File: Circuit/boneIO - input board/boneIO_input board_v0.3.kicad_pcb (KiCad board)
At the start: 2 copper layers, 256 x 74 mm, 264 parts, among them J1 Screw_Terminal_01x08, J10 Screw_Terminal_01x08, J11 Screw_Terminal_01x08, J12 ZW_VCC, J13 ZW_GND, J14 INNY ZASILACZ, J15 BeagleBone_Black_Header, J16 BeagleBone_Black_Header, J2 Screw_Terminal_01x08, J3 Screw_Terminal_01x08, J4 Screw_Terminal_01x08, J5 Screw_Terminal_01x08, J6 Screw_Terminal_01x08, J7 Screw_Terminal_01x08, J8 Screw_Terminal_01x04, J9 Conn_02x04_Odd_Even, SW1 SW_Push, U1 P82B96, U10 LM2596S-ADJ, U11 RS485, U12 PC817X2NIP0F, U13 PC817X2NIP0F, U14 PC817X2NIP0F, U15 PC817X2NIP0F, U16 PC817X2NIP0F, U17 PC817X2NIP0F, U18 PC817X2NIP0F, U19 PC817X2NIP0F, U2 PC817X2NIP0F, U20 PC817X2NIP0F, U21 PC817X2NIP0F, U22 PC817X2NIP0F, U23 PC817X2NIP0F, U24 PC817X2NIP0F, U25 PC817X2NIP0F, U26 PC817X2NIP0F, U27 PC817X2NIP0F, U28 PC817X2NIP0F, U29 PC817X2NIP0F, U3 PC817X2NIP0F, U30 PC817X2NIP0F, U31 PC817X2NIP0F, U32 PC817X2NIP0F, U33 PC817X2NIP0F, U34 PC817X2NIP0F, U35 PC817X2NIP0F, U36 DS1307Z+, U37 PC817X2NIP0F, U38 PC817X2NIP0F, U39 PC817X2NIP0F, U4 PC817X2NIP0F, U40 PC817X2NIP0F, U41 PC817X2NIP0F, U42 PC817X2NIP0F, U43 PC817X2NIP0F, U44 PC817X2NIP0F, U45 PC817X2NIP0F, U46 PC817X2NIP0F, U47 PC817X2NIP0F, U48 PC817X2NIP0F, U49 PC817X2NIP0F, U5 PC817X2NIP0F, U50 PC817X2NIP0F, U51 PC817X2NIP0F, U52 PC817X2NIP0F, U53 PC817X2NIP0F, U54 PC817X2NIP0F, U55 PC817X2NIP0F, U56 PC817X2NIP0F, U6 PC817X2NIP0F, U7 PC817X2NIP0F, U8 PC817X2NIP0F, U9 PC817X2NIP0F, Y1 32,788 MHz

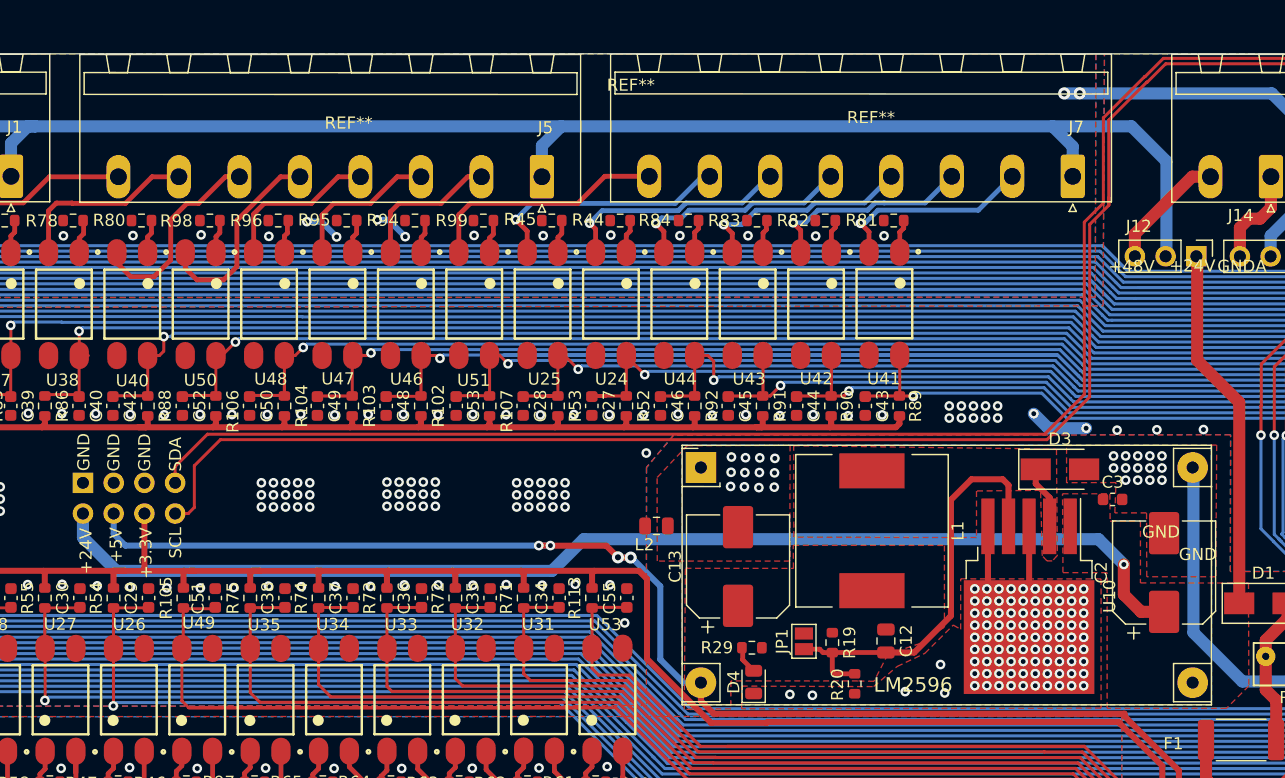
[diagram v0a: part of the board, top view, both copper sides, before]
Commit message: Wymiana gniazda
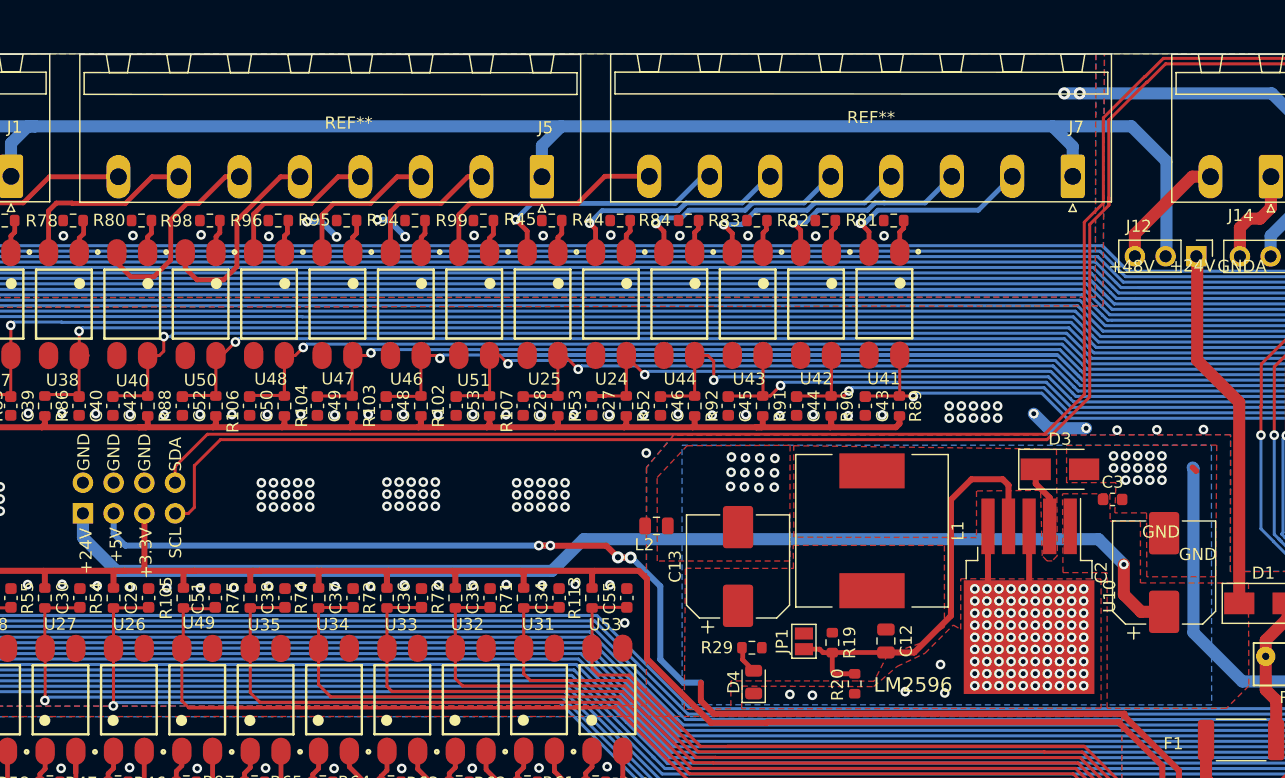
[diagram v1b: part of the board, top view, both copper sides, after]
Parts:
- removed REF**: YAAJ_DCDC_StepDown_LM2596, Module:YAAJ_DCDC_StepDown_LM2596
- J9: footprint Connector_PinHeader_2.54mm:PinHeader_2x04_P2.54mm_Vertical -> Connector_PinSocket_2.54mm:PinSocket_2x04_P2.54mm_Vertical
- moved J9 2.53 mm to (109.6, 84.3)
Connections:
- J9 pad 1: GND -> +24V
- J9 pad 2: +24V -> GND
- J9 pad 3: GND -> +5V
- J9 pad 4: +5V -> GND
- J9 pad 5: GND -> +3V3
- J9 pad 6: +3V3 -> GND
- J9 pad 7: SDA -> SCL
- J9 pad 8: SCL -> SDA
